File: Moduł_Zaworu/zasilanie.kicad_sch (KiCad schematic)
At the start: 26 parts, among them J1 Screw_Terminal_01x03, J5 Screw_Terminal_01x02, J6 Screw_Terminal_01x02, J7 Screw_Terminal_01x02, U1 TL431D, U2 INA219AxD, U3 L7805, U4 TLV172IDCK, U5 LD1117S33TR_SOT223

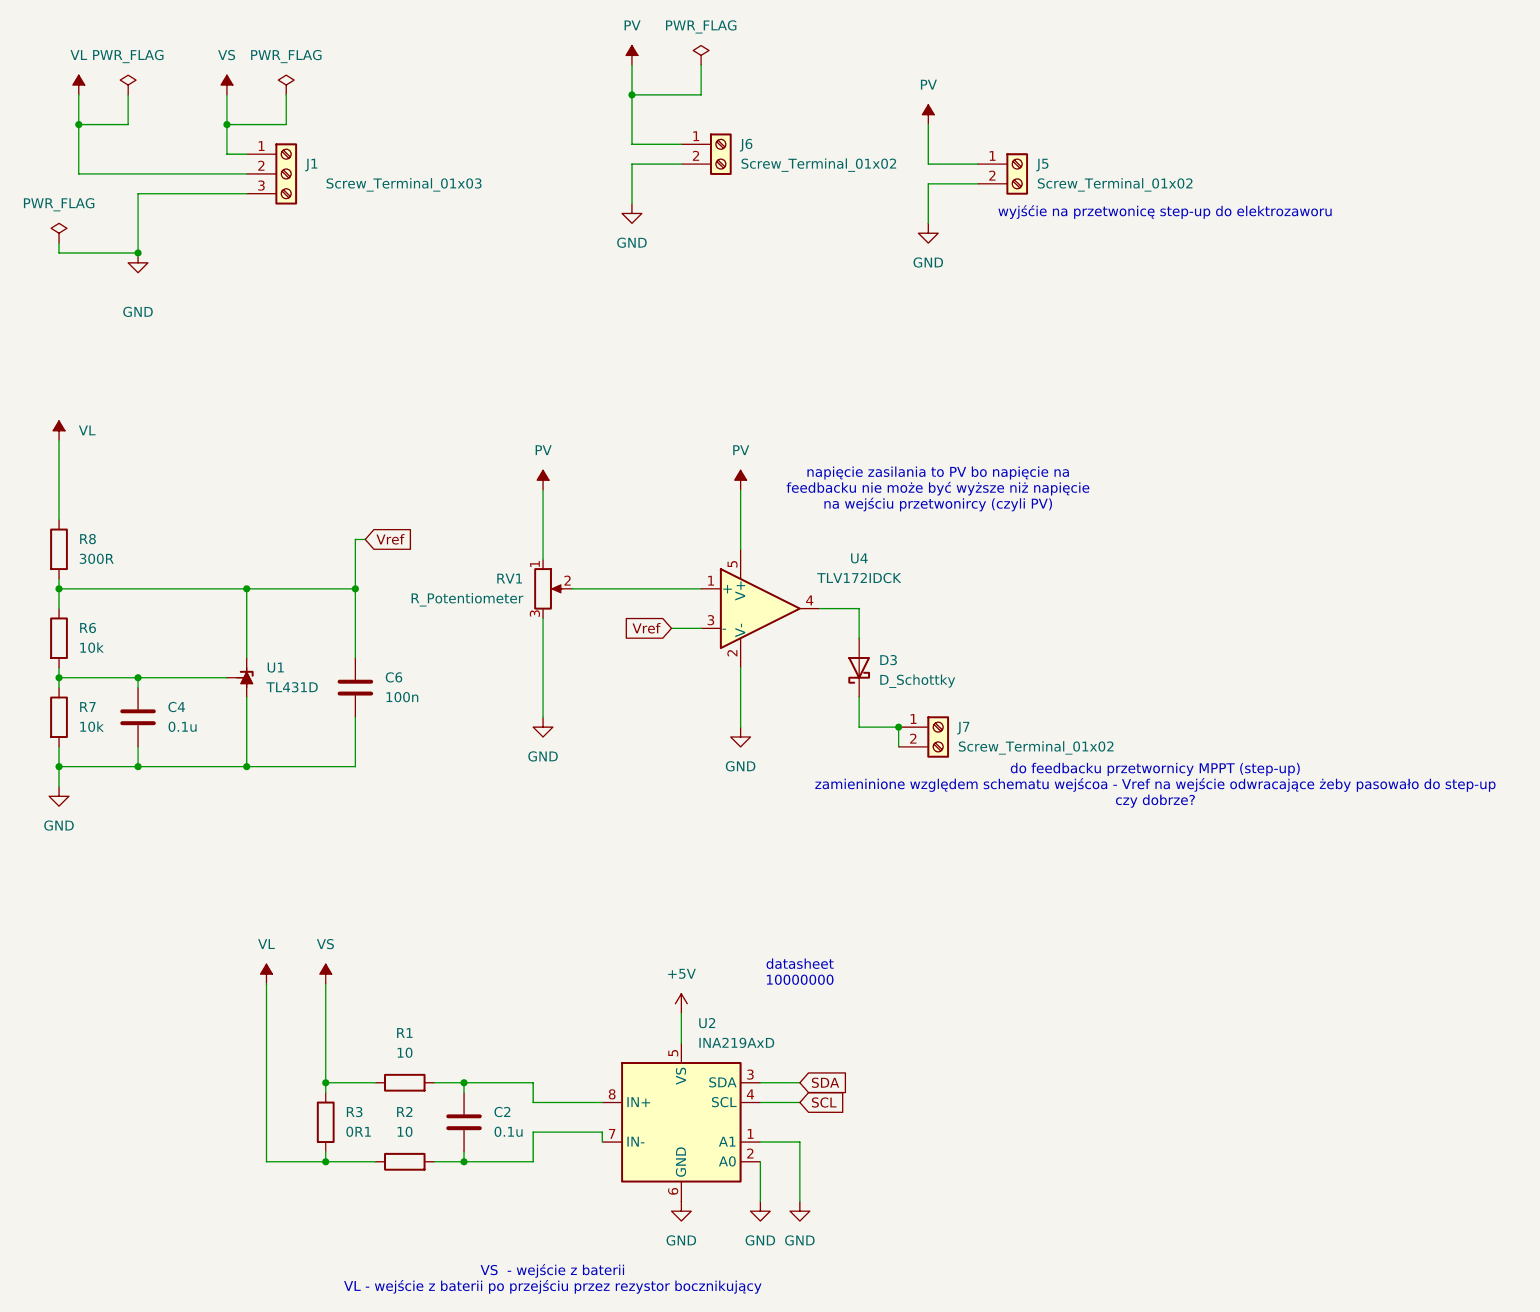
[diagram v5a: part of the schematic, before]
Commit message: Testing MQTT + apllikacja webowa+ baza danych. Dodanie zworek pozwalaąjcych na zaminę trybu przetwornicy mppt, zmiana układu zasilania zgodnie z zaleceniami Pana Mariusza.
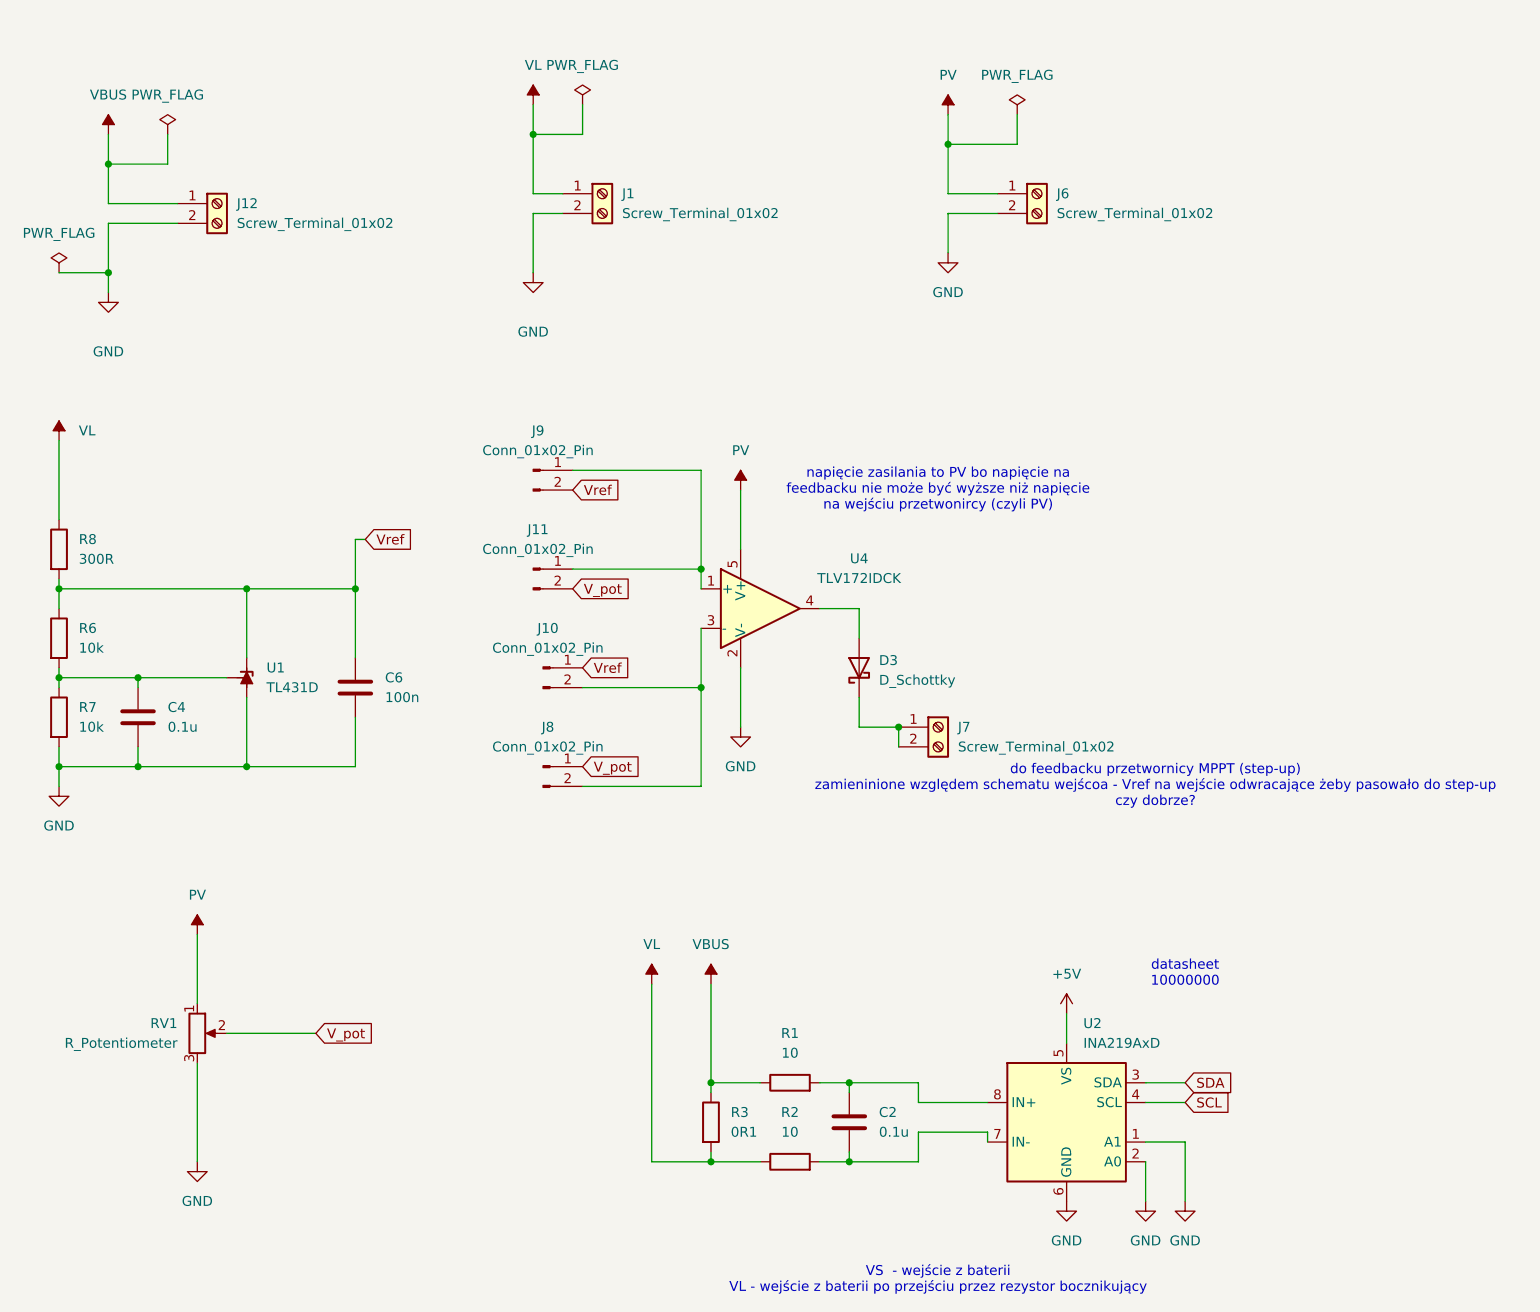
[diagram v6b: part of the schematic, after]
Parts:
- removed J1: Screw_Terminal_01x03, TerminalBlock:TerminalBlock_MaiXu_MX126-5.0-03P_1x03_P5.00mm, symbol Connector:Screw_Terminal_01x03
- removed J5: Screw_Terminal_01x02, TerminalBlock:TerminalBlock_MaiXu_MX126-5.0-02P_1x02_P5.00mm, symbol Connector:Screw_Terminal_01x02
- added J1, J12: Screw_Terminal_01x02, TerminalBlock:TerminalBlock_MaiXu_MX126-5.0-02P_1x02_P5.00mm, symbol Connector:Screw_Terminal_01x02
- added J10, J11, J8, J9: Conn_01x02_Pin, Connector_PinHeader_2.54mm:PinHeader_1x02_P2.54mm_Vertical, symbol Connector:Conn_01x02_Pin
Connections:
- net GND: now also J1.2 (Pin_2), J12.2 (Pin_2)
- net VL: now also J1.1 (Pin_1)
- net Vref: now also J10.1 (Pin_1), J9.2 (Pin_2); no longer U4.3 (-)
- net at U4.1 (+): now also J11.1 (Pin_1), J9.1 (Pin_1); no longer RV1.2
- net VS renamed VBUS
- net VBUS: now also J12.1 (Pin_1)
- new net: J10.2 (Pin_2), J8.2 (Pin_2), U4.3 (-)
- new net V_pot: J11.2 (Pin_2), J8.1 (Pin_1), RV1.2
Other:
- note removed: "wyjśćie na przetwonicę step-up do elektrozaworu"
- moved on the sheet: C2, J6, R1, R2, R3, RV1, U2

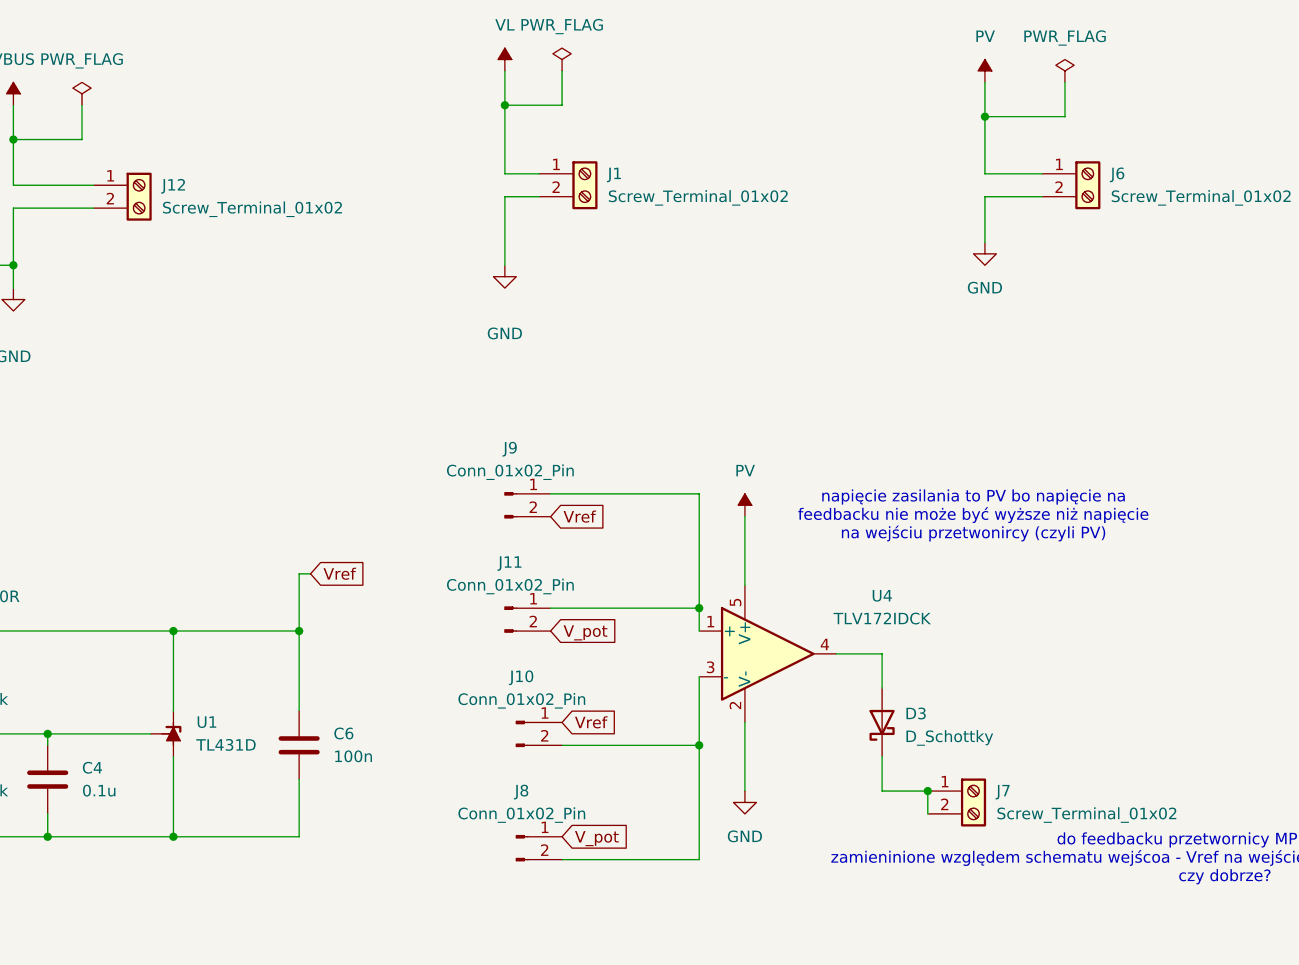
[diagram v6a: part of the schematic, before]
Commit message: Kod websocket, kod stonka demo, kod sterownika - wszystkie taski poza bt wstepnie ogarniete
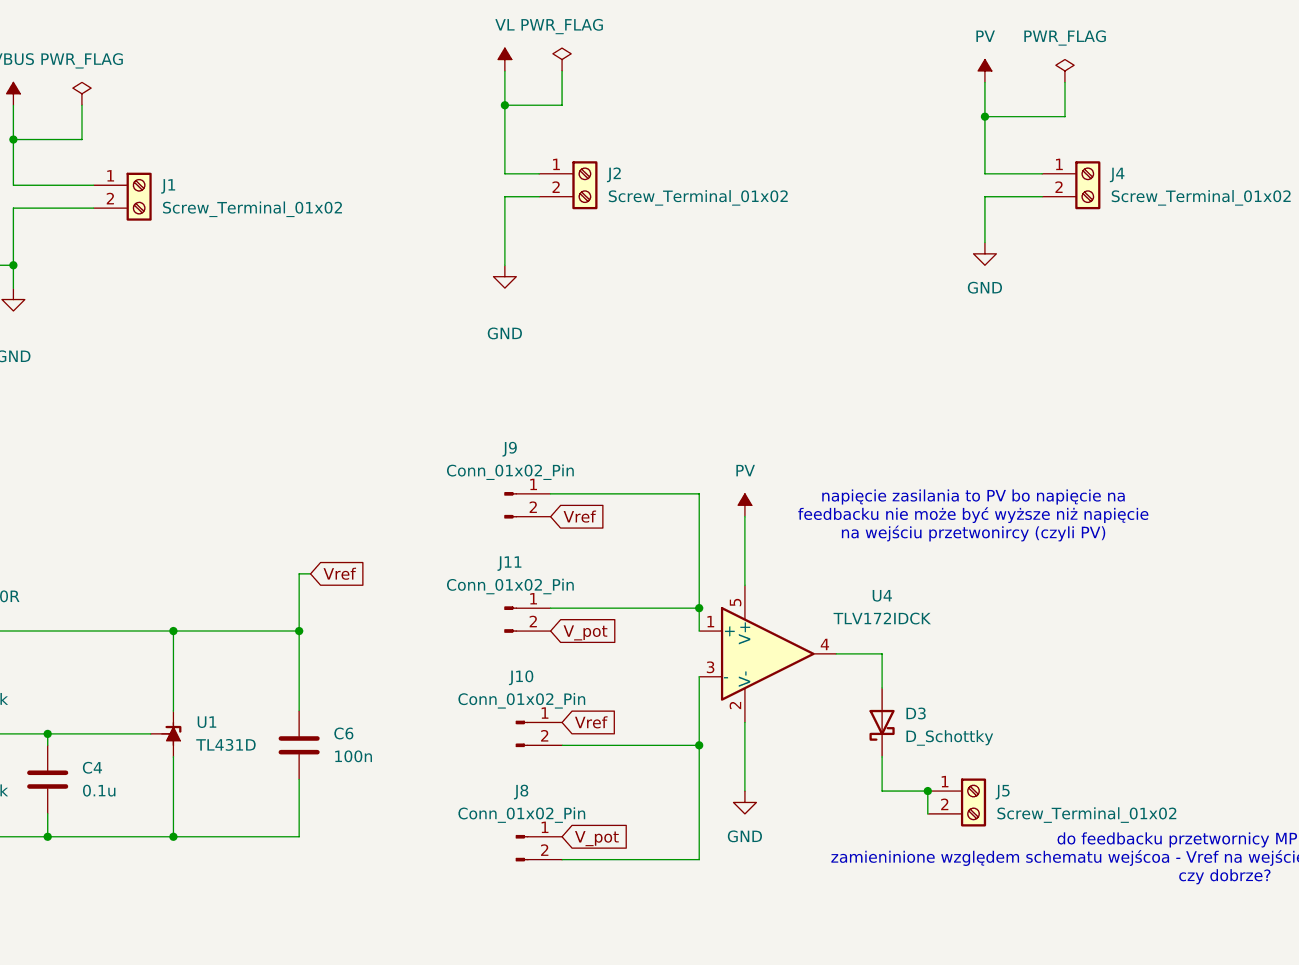
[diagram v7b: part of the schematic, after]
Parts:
- renumbered J12 to J1, J1 to J2, J6 to J4, J7 to J5
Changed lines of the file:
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@@
 		(dnp no)
 		(fields_autoplaced yes)
-		(property "Reference" "J1"
+		(property "Reference" "J2"
 			(at 93.98 39.3699 0)
 			(effects
@@
 			(project "Moduł_Zaworu"
 				(path "/8513fd68-b07b-4062-94bb-7b0327ec704f/94594dad-4c19-4a9b-a7b2-827222d80e0d"
-					(reference "J1")
+					(reference "J2")
 					(unit 1)
 				)
@@
 		(on_board yes)
 		(dnp no)
-		(property "Reference" "J6"
+		(property "Reference" "J4"
 			(at 149.86 39.3699 0)
 			(effects
@@
 			(project "Moduł_Zaworu"
 				(path "/8513fd68-b07b-4062-94bb-7b0327ec704f/94594dad-4c19-4a9b-a7b2-827222d80e0d"
-					(reference "J6")
+					(reference "J4")
 					(unit 1)
 				)
@@
 		(dnp no)
 		(fields_autoplaced yes)
-		(property "Reference" "J7"
+		(property "Reference" "J5"
 			(at 137.16 107.9499 0)
 			(effects
@@
 			(project "Moduł_Zaworu"
 				(path "/8513fd68-b07b-4062-94bb-7b0327ec704f/94594dad-4c19-4a9b-a7b2-827222d80e0d"
-					(reference "J7")
+					(reference "J5")
 					(unit 1)
 				)
@@
 		(on_board yes)
 		(dnp no)
-		(property "Reference" "J12"
+		(property "Reference" "J1"
 			(at 44.45 40.6399 0)
 			(effects
@@
 			(project "Moduł_Zaworu"
 				(path "/8513fd68-b07b-4062-94bb-7b0327ec704f/94594dad-4c19-4a9b-a7b2-827222d80e0d"
-					(reference "J12")
-					(unit 1)
-				)
+					(reference "J1")
+					(unit 1)
+				)
